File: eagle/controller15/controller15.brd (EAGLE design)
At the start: 30 x 65 mm, 68 parts, among them IC1 MCP170312MB, IC3 FE1.1S, Q2 200mA/50V, Q4 200mA/50V, Q6 200mA/50V, Q8 200mA/50V, U1 ATSAMD21G-A, U3 MP2307, Y2 32.768

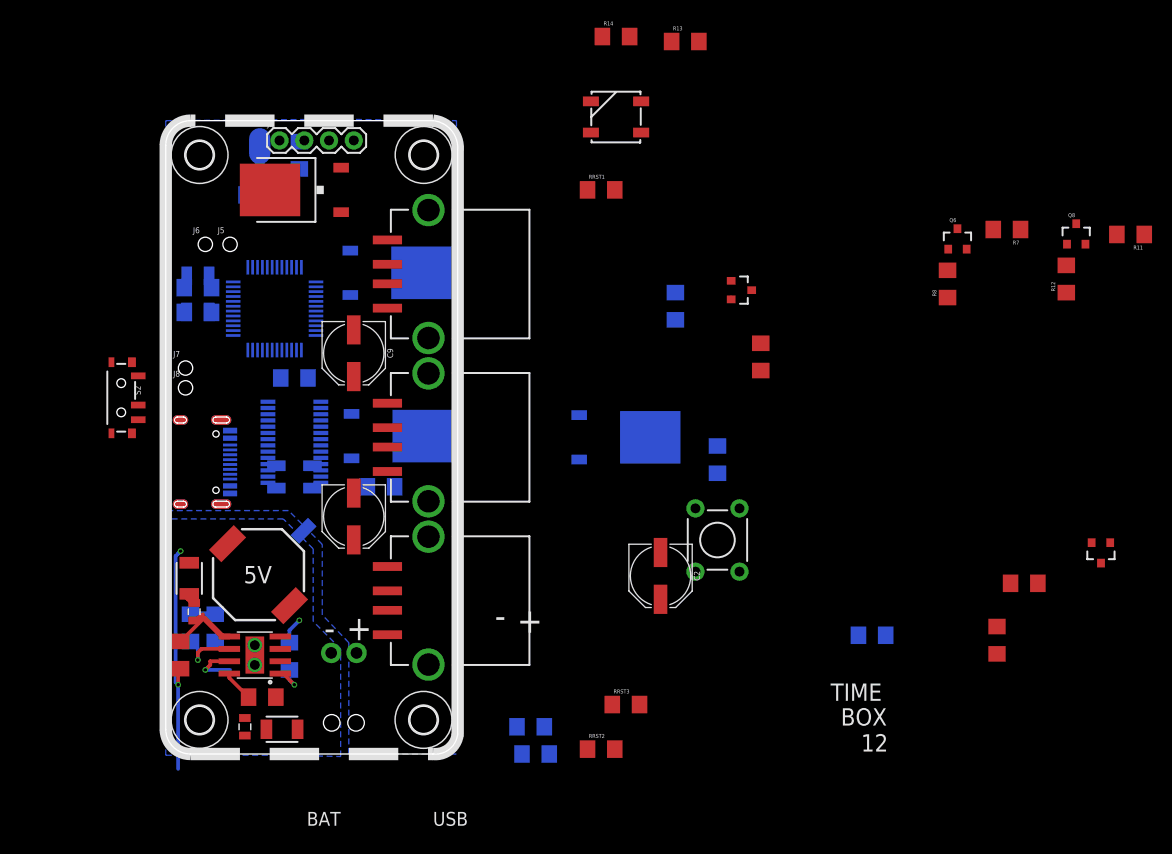
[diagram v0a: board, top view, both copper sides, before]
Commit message: controller15 board files nearly finished usbDirectController3 firmware
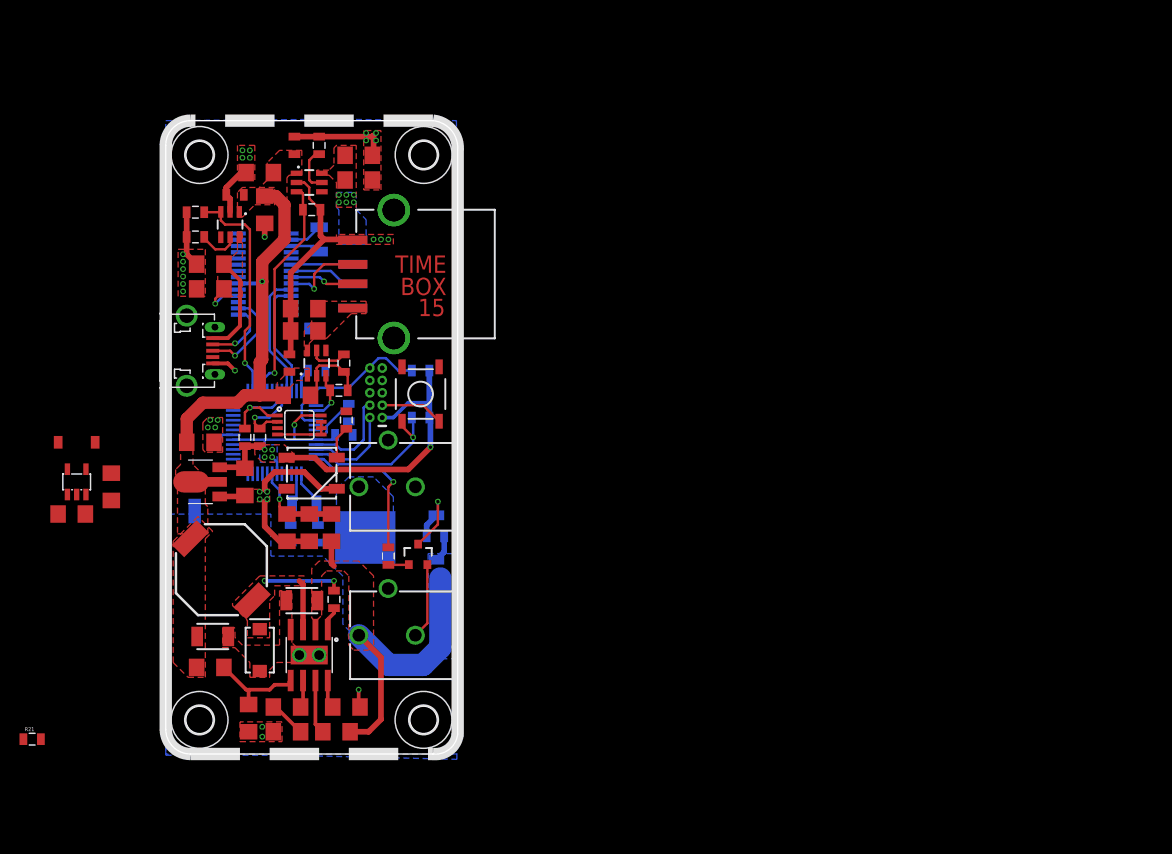
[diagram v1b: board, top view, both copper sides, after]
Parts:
- removed J1: (no value), SparkFun-Connectors:USB-C-16P
- removed J5, J6, J7, J8: (no value), SparkFun-Connectors:1X01_POGOPIN_HOLE_0.58_DIA
- removed Q1, Q5, Q7: (no value), transistor-fet:TO252
- removed Q2, Q6, Q8: 200mA/50V, SparkFun-DiscreteSemi:SOT23-3
- removed R10, R12, R8: 1k, SparkFun-Resistors:1206
- removed R11, R7, R9: 10k, SparkFun-Resistors:1206
- removed R13, R14: 5.1k, SparkFun-Passives:1206
- removed RRST2, RRST3: (no value), SparkFun-Passives:1206
- removed S2: (no value), SparkFun-Switches:SWITCH_SPST_SMD_A
- removed U$4: NANOFIT2, volzolib:NANOFIT2
- removed USB_3: USB_A_SMT_FEMALE, SparkFun-Connectors:USB-A-S-SILK-FEMALE
- added AP1, AP2, AP2553: MCP4725, SparkFun-IC-Conversion:SOT23-6
- added C10, C21, C27, C3: 10uF, SparkFun-Capacitors:1206
- added C11, C17, C22, C25: 0.1uF, SparkFun-Capacitors:0805
- added C12, C18, C23: 1.0uF, SparkFun-Capacitors:1206
- added C20, C24: 120uF, SparkFun-Capacitors:1206
- added C26: 4.7uF, SparkFun-Capacitors:1206
- added D1: 3A/40V/500mV, SparkFun-DiscreteSemi:SMA-DIODE
- added J3, J4: POWER_JACKPTH_BREAD, SparkFun-Connectors:POWER_JACK_PTH_BREAD
- added L1: 2.2µH/±20%/1.5A, SparkFun-Coils:INDUCTOR_2.2UH
- added LM3671: MCP73811/2, adafruit:SOT23-5L
- added MCP9808: V_REG_MIC5216, SparkFun-IC-Power:MSOP8
- added R21: (no value), SparkFun-Passives:0805
- added R_I2C_1, R_I2C_2, R_MOSFET_USB3, R_MOSFET_USB4, R_MOSFET_USB6: 10k, SparkFun-Passives:0805
- added R_MOSFET_USB1, R_MOSFET_USB2, R_MOSFET_USB5: ? (1%), SparkFun-Passives:0805
- added X2: ZX62D-B-5PA8, zx62d-b-5pa8-oshpark_10:ZX62D-B-5PA8
- C1, C9: value 100uF -> 0.1uF; device SparkFun-Capacitors:PANASONIC_D -> SparkFun-Capacitors:0805
- C13: device SparkFun-Capacitors:1206 -> SparkFun-Capacitors:0805
- C2: value 100uF -> 120uF; device SparkFun-Capacitors:PANASONIC_D -> SparkFun-Capacitors:1206
- C4, C5, R5, REXT, RRST1: device SparkFun-Passives:1206 -> SparkFun-Passives:0805
- J2: value (none) -> CORTEX_DEBUG_PTH; device SparkFun-Connectors:1X04 -> SparkFun-Connectors:2X5-PTH-1.27MM
- R2, R24: device SparkFun-Resistors:0805 -> SparkFun-Resistors:1206
- R4, R6, R_LED: device SparkFun-Resistors:1206 -> SparkFun-Resistors:0805
- S1: device SparkFun-Retired:TACTILE-PTH -> SparkFun-Retired:TACTILE-SWITCH-SMD
- Y1: value (none) -> 32.768kHz; device SparkFun-FreqCtrl:CRYSTAL-SMD-5X3 -> SparkFun-FreqCtrl:CRYSTAL-SMD-3.2X1.5MM
- Y2: value 32.768 -> 32.768kHz; device SparkFun-FreqCtrl:CRYSTAL-SMD-5X3 -> SparkFun-FreqCtrl:CRYSTAL-SMD-3.2X1.5MM
- moved Q4 70.1 mm to (25.9, 20.4), turned to 0 degrees
- moved R6 63.1 mm to (22.9, 20.3)
- moved C6 61.1 mm to (12.4, 23.2), flipped to the top, turned to 270 degrees
- moved R4 60.6 mm to (27.7, 22.4), flipped to the bottom
- moved D2 48.1 mm to (15.0, 28.8), turned to 0 degrees
- moved C2 45.7 mm to (14.2, 45.7), turned to 0 degrees
- moved R_LED 35.7 mm to (18.5, 34.3), flipped to the top, turned to 270 degrees
- moved IC1 34.1 mm to (3.56, 27.9), flipped to the top, turned to 90 degrees
- moved S1 34.0 mm to (26.2, 37.0), turned to 270 degrees
- moved VD1 31.3 mm to (17.0, 23.2), flipped to the top, turned to 270 degrees
- moved C7 31.2 mm to (3.56, 32.0), flipped to the top, turned to 0 degrees
- moved R5 30.8 mm to (26.2, 34.5), turned to 0 degrees
- moved VD2 30.6 mm to (14.7, 23.2), flipped to the top, turned to 90 degrees
- moved C8 29.5 mm to (8.13, 27.9), flipped to the top, turned to 270 degrees
- moved C4 28.1 mm to (15.6, 22.6), turned to 90 degrees
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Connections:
- removed net BATT_VD: RRST2.1, RRST3.2
- removed net CC1: J1.A5, R14.2
- removed net CC2: J1.B5, R13.2
- removed net HUB_1: Q3.3
- removed net HUB_1_EN: R6.1
- removed net HUB_2: Q1.3
- removed net HUB_2_EN: R10.1
- removed net HUB_3: Q5.3
- removed net HUB_3_EN: R8.1
- removed net HUB_ZERO: Q7.3
- removed net HUB_ZERO_EN: R12.1
- removed net N$12: Q5.1, Q6.3, R7.2
- removed net N$13: Q6.1, R8.2
- removed net N$15: Q7.1, Q8.3, R11.2
- removed net N$19: Q8.1, R12.2
- removed net N$21: RRST1.1, U1.40
- removed net N$34: C1.-, USB_2.VBUS
- removed net N$35: C9.-, USB_1.VBUS
- removed net N$40: C2.-, USB_3.VBUS
- removed net N$6: Q2.1, R10.2
- removed net SHLD: J1.SHLD1, J1.SHLD2, J1.SHLD3, J1.SHLD4, J1.SHLD5, J1.SHLD6, J1.SHLD7, J1.SHLD8
- removed net USB_5V: J1.VBUS1, J1.VBUS2, S2.3
- removed net ZERO_DM: IC3.15, J1.A7, J1.B7, J8.1
- removed net ZERO_DP: IC3.16, J1.A6, J1.B6, J7.1
- new net CAM_EN: R6.1, U1.48
- new net CAM_OUT: J3.PWR, Q3.3
- new net EN: LM3671.3, R21.1
- new net MICRO_DM: IC3.15, X2.2
- new net MICRO_DP: IC3.16, X2.3
- new net MICRO_VBUS: AP2.6, C23.2, C24.2, IC3.18, X2.1
- new net N$10: AP1.5, R_MOSFET_USB2.2
- new net N$11: AP2.5, R_MOSFET_USB5.2
- new net RESET: J2.10, RRST1.1, U1.40
- new net SCL: MCP9808.2, R_I2C_1.2, U1.32
- new net SDA: MCP9808.1, R_I2C_2.1, U1.31
- new net USB0_EN: AP2.3, R_MOSFET_USB6.2, U1.26
- new net USB1_EN: AP2553.3, R_MOSFET_USB3.2, U1.38
- new net USB1_OUT: AP2553.6, C12.2, C2.2, USB_1.VBUS
- new net USB2_EN: AP1.3, R_MOSFET_USB4.2, U1.28
- new net USB2_OUT: AP1.6, C18.2, C20.2, USB_2.VBUS
- net BATT_VCC: now also J4.PWR, Q3.2, R4.1; no longer RRST2.2, U$4.P$2
- net BTN: now also U1.47
- net CONV_5V: now also C26.2, LM3671.1, R21.2; no longer IC3.20, S2.1
- net GND: now also AP1.2, AP2.2, AP2553.2, C1.2, C10.2, C11.2, C12.1, C17.2, C18.1, C2.1, C20.1, C21.2, C22.2, C23.1, C24.1, C25.1, C26.1, C27.2, C3.2, C9.2, J2.3, J2.5, J3.GND, J4.GND, LM3671.2, MCP9808.4, MCP9808.5, MCP9808.6, MCP9808.7, R_MOSFET_USB1.1, R_MOSFET_USB2.1, R_MOSFET_USB3.1, R_MOSFET_USB4.1, R_MOSFET_USB5.1, R_MOSFET_USB6.1, X2.5; no longer J1.GND, J1.GND2, J2.1, Q2.2, Q6.2, Q8.2, R13.1, R14.1, RRST3.1, U$4.P$1, USB_3.GND
- net GNDA: now also D1.A
- net LED: now also U1.15
- net N$1: now also L1.P$1, LM3671.5; no longer Q1.1, Q2.3, R9.2
- net N$23: now also Y2.P$1; no longer Y2.1
- net N$24: now also Y2.P$2; no longer Y2.3
- net N$26: now also D1.C
- net N$32: now also Y1.P$1; no longer Y1.1
- net N$4: now also MCP9808.3; no longer C9.+
- net N$5: now also C25.2, U1.43; no longer C1.+
- net N$8: now also Y1.P$2; no longer Y1.3
- net N$9: now also AP2553.5, R_MOSFET_USB1.2; no longer C2.+
- net SWDCLK: now also J2.4; no longer J2.2
- net SWDIO: now also J2.2; no longer J2.3
- net USB_3_DM: no longer USB_3.D-
- net USB_3_DP: no longer USB_3.D+
- net VCC: now also C1.1, C27.1, C9.1, J2.1, L1.P$2, LM3671.4, MCP9808.8, R_I2C_1.1, R_I2C_2.2; no longer J2.4, U1.43
- net VCC_5V: now also AP1.1, AP2.1, AP2553.1, C10.1, C11.1, C17.1, C21.1, C22.1, C3.1, IC3.20; no longer Q1.2, Q3.2, Q5.2, Q7.2, R11.1, R4.1, R7.1, R9.1, S2.2
- net VD_INT: now also U1.7
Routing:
- net GND: track 0.65 -> 100.0 mm, vias 0 -> 27
- net VCC: track 0.00 -> 57.1 mm, vias 0 -> 6
- net VCC_5V: track 0.00 -> 38.9 mm, vias 0 -> 1
- net BATT_VCC: track 0.51 -> 36.1 mm
- net CONV_5V: track 24.8 -> 0.00 mm, vias 2 -> 0
- net USB2_EN: track 0.00 -> 23.1 mm, vias 0 -> 1
- net USB0_EN: track 0.00 -> 23.1 mm, vias 0 -> 1
- net RESET: track 0.00 -> 16.8 mm
- net BTN: track 0.00 -> 16.0 mm, vias 0 -> 1
- net CAM_EN: track 0.00 -> 15.8 mm, vias 0 -> 1
- net MICRO_VBUS: track 0.00 -> 14.9 mm, vias 0 -> 1
- net UC_DM: track 0.00 -> 12.9 mm
- net UC_DP: track 0.00 -> 12.0 mm
- net N$26: track 2.70 -> 13.3 mm, vias 1 -> 2
- net MICRO_DP: track 0.00 -> 9.79 mm, vias 0 -> 1
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- added copper zone on layer 1, net BATT_VCC
- added copper zone on layer 16, net BATT_VCC
- added copper zone on layer 16, net CAM_OUT
- added copper zone on layer 1, net CONV_5V
- added copper zone on layer 1, net GND
- added copper zone on layer 1, net GNDA
- added copper zone on layer 1, net MICRO_VBUS
- added copper zone on layer 1, net N$26
- added copper zone on layer 1, net USB1_OUT
- added copper zone on layer 1, net USB2_OUT
- added copper zone on layer 16, net USB2_OUT
- added copper zone on layer 1, net VCC
- added copper zone on layer 16, net VCC
- added copper zone on layer 1, net VCC_5V
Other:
- board text added: "15"
- board text added: "IN"
- board text added: "OUT"
- board text removed: "+"
- board text removed: "-"
- board text removed: "12"
- board text removed: "5V"
- board text removed: "BAT"
- board text removed: "USB"

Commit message: minor changes
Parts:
- C25: value 0.1uF -> 1.0uF
- R_LED: value 4.7k -> 470
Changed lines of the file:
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@@
 <attribute name="VALUE" x="19.24" y="27.229" size="0.6096" layer="27"/>
 </element>
-<element name="R_LED" library="SparkFun-Resistors" package="0805" value="4.7k" x="18.542" y="34.29" smashed="yes" rot="R270"/>
+<element name="R_LED" library="SparkFun-Resistors" package="0805" value="470" x="18.542" y="34.29" smashed="yes" rot="R270"/>
 <element name="C13" library="SparkFun-Capacitors" package="0805" value="10nF" x="17.272" y="15.875" smashed="yes" rot="R90"/>
 <element name="R1" library="SparkFun-Resistors" package="1206" value="6.8k" x="12.446" y="2.286" smashed="yes" rot="R180"/>
@@
 <attribute name="VALUE" x="18.288" y="33.655" size="0.6096" layer="28" font="vector" ratio="20" rot="MR180" align="top-center"/>
 </element>
-<element name="C25" library="SparkFun-Capacitors" library_urn="urn:adsk.eagle:library:510" package="0805" package3d_urn="urn:adsk.eagle:package:37429/1" value="0.1uF" x="18.796" y="35.052" smashed="yes" rot="MR90">
+<element name="C25" library="SparkFun-Capacitors" library_urn="urn:adsk.eagle:library:510" package="0805" package3d_urn="urn:adsk.eagle:package:37429/1" value="1.0uF" x="18.796" y="35.052" smashed="yes" rot="MR90">
 <attribute name="PROD_ID" value="CAP-08064" x="18.796" y="35.052" size="1.778" layer="28" rot="MR90" display="off"/>
 <attribute name="VALUE" x="17.907" y="35.052" size="0.6096" layer="28" font="vector" ratio="20" rot="MR90" align="top-center"/>
@@
 <wire x1="13.929" y1="34.757" x2="13.926" y2="37.27" width="0" layer="19" extent="1-16"/>
 <wire x1="-5.588" y1="28.832" x2="5.537" y2="29.439" width="0" layer="19" extent="1-1"/>
-<wire x1="-7.244" y1="32.004" x2="-5.588" y2="28.832" width="0" layer="19" extent="1-1"/>
-<wire x1="-8.194" y1="29.24" x2="-7.244" y2="32.004" width="0" layer="19" extent="1-1"/>
+<wire x1="-8.194" y1="29.24" x2="-5.588" y2="28.832" width="0" layer="19" extent="1-1"/>
+<wire x1="-7.244" y1="32.004" x2="-8.194" y2="29.24" width="0" layer="19" extent="1-1"/>
 </signal>
 <signal name="GND">
@@
 <wire x1="19.188" y1="32.766" x2="18.796" y2="34.152" width="0" layer="19" extent="16-16"/>
 <wire x1="-5.588" y1="26.032" x2="2.9718" y2="25.5778" width="0" layer="19" extent="1-16"/>
-<wire x1="-9.144" y1="26.64" x2="-5.588" y2="26.032" width="0" layer="19" extent="1-1"/>
-<wire x1="-8.252" y1="24.638" x2="-9.144" y2="26.64" width="0" layer="19" extent="1-1"/>
+<wire x1="-8.252" y1="24.638" x2="-5.588" y2="26.032" width="0" layer="19" extent="1-1"/>
+<wire x1="-9.144" y1="26.64" x2="-8.252" y2="24.638" width="0" layer="19" extent="1-1"/>
 </signal>
 <signal name="BATT_VCC" class="2">

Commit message: controller15 sent to fab
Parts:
- removed C26: 4.7uF, SparkFun-Capacitors:1206
- removed C27: 10uF, SparkFun-Capacitors:1206
- removed L1: 2.2µH/±20%/1.5A, SparkFun-Coils:INDUCTOR_2.2UH
- removed LM3671: MCP73811/2, adafruit:SOT23-5L
- removed R21: (no value), SparkFun-Passives:0805
- added C28, C29: 10uF, SparkFun-Capacitors:0805
- added R7: 10k, SparkFun-Passives:0805
- REXT: value 2.7k -> 2.7k / 1%
- Y2: value 32.768kHz -> 12MHz
- moved REXT 1.93 mm to (14.5, 41.9), turned to 90 degrees
- moved C25 0.80 mm to (18.0, 35.3), turned to 270 degrees
- moved R_LED 0.72 mm to (18.0, 33.8)
- moved R_MOSFET_USB1 0.25 mm to (18.0, 40.1)
- moved C9 0.25 mm to (15.7, 39.4)
- moved R_I2C_1 0.25 mm to (9.65, 32.3)
- moved R_I2C_2 0.25 mm to (8.13, 32.3)
- moved R_MOSFET_USB3 0.25 mm to (17.8, 37.1)
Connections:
- removed net EN: LM3671.3, R21.1
- removed net N$1: L1.P$1, LM3671.5
- new net N$15: IC3.17, R7.1
- new net VD_18: C28.1, IC3.12, IC3.28
- new net VD_33: C29.2, IC3.13, IC3.19, IC3.21, IC3.26, R7.2
- net CAM_EN: now also U1.10; no longer U1.48
- net CONV_5V: no longer C26.2, LM3671.1, R21.2
- net GND: now also C28.2, C29.1, IC3.27; no longer C26.1, C27.2, LM3671.2
- net LED: now also U1.27; no longer U1.15
- net USB1_EN: now also U1.30; no longer U1.38
- net VCC: no longer C27.1, L1.P$2, LM3671.4
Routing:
- net VD_33: track 0.00 -> 62.9 mm
- net VD_18: track 0.00 -> 43.8 mm
- net GND: track 100.0 -> 128.3 mm, vias 27 -> 28
- net N$15: track 0.00 -> 11.4 mm
- net LED: track 0.00 -> 10.4 mm, vias 0 -> 1
- net VCC: track 57.1 -> 65.7 mm, vias 6 -> 5
- net USB1_EN: track 4.92 -> 10.6 mm
- net CAM_EN: track 15.8 -> 18.6 mm
- net MICRO_VBUS: track 14.9 -> 17.4 mm
- net RESET: track 16.8 -> 19.3 mm, vias 0 -> 1
- net N$31: track 1.45 -> 2.97 mm
- net N$5: track 5.07 -> 3.55 mm
- net N$7: track 3.41 -> 2.65 mm
